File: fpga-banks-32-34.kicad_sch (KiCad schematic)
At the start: 11 parts, among them U4 XC7K160T-FFG676, Y3 Oscillator_100MHz_ASFL1

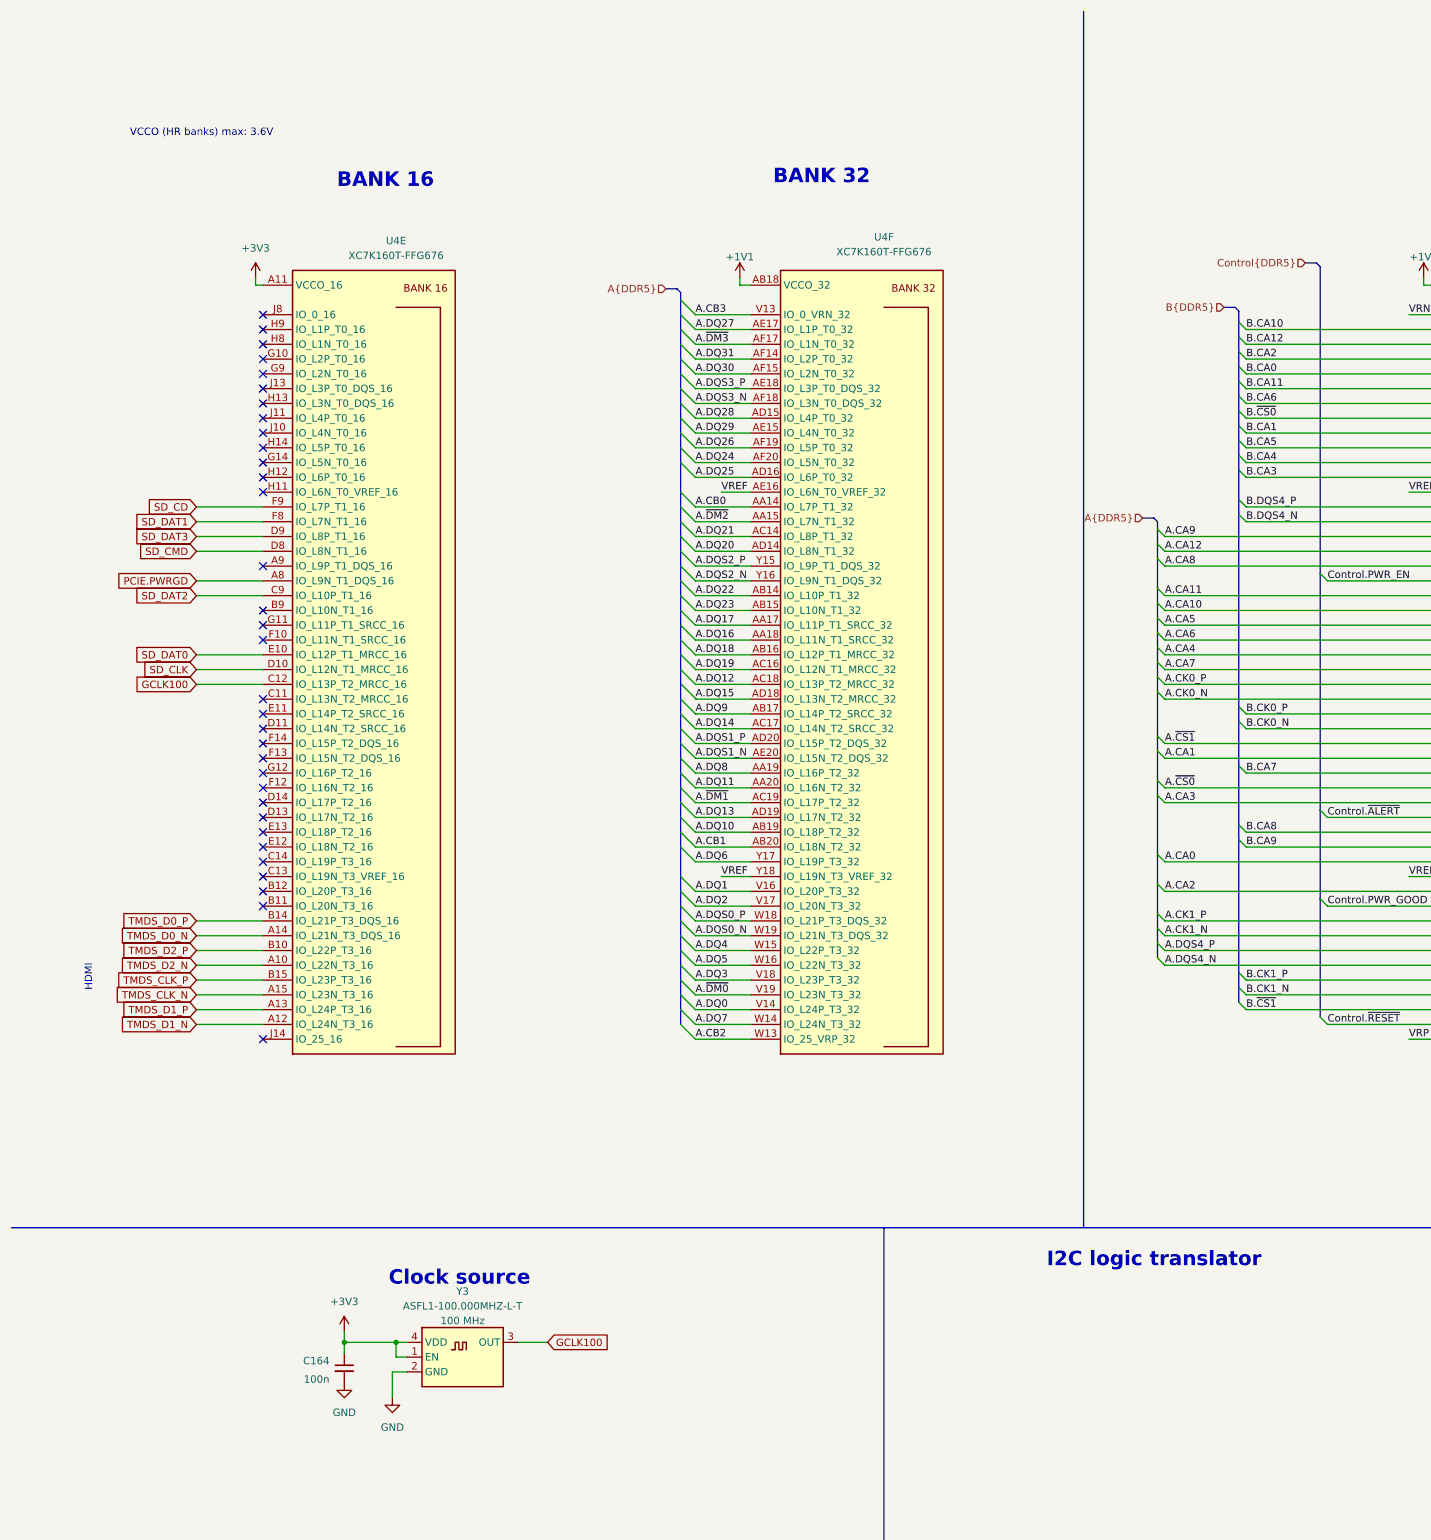
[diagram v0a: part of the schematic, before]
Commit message: Finish creating hierarchical buses and structure, start reconnecting signals
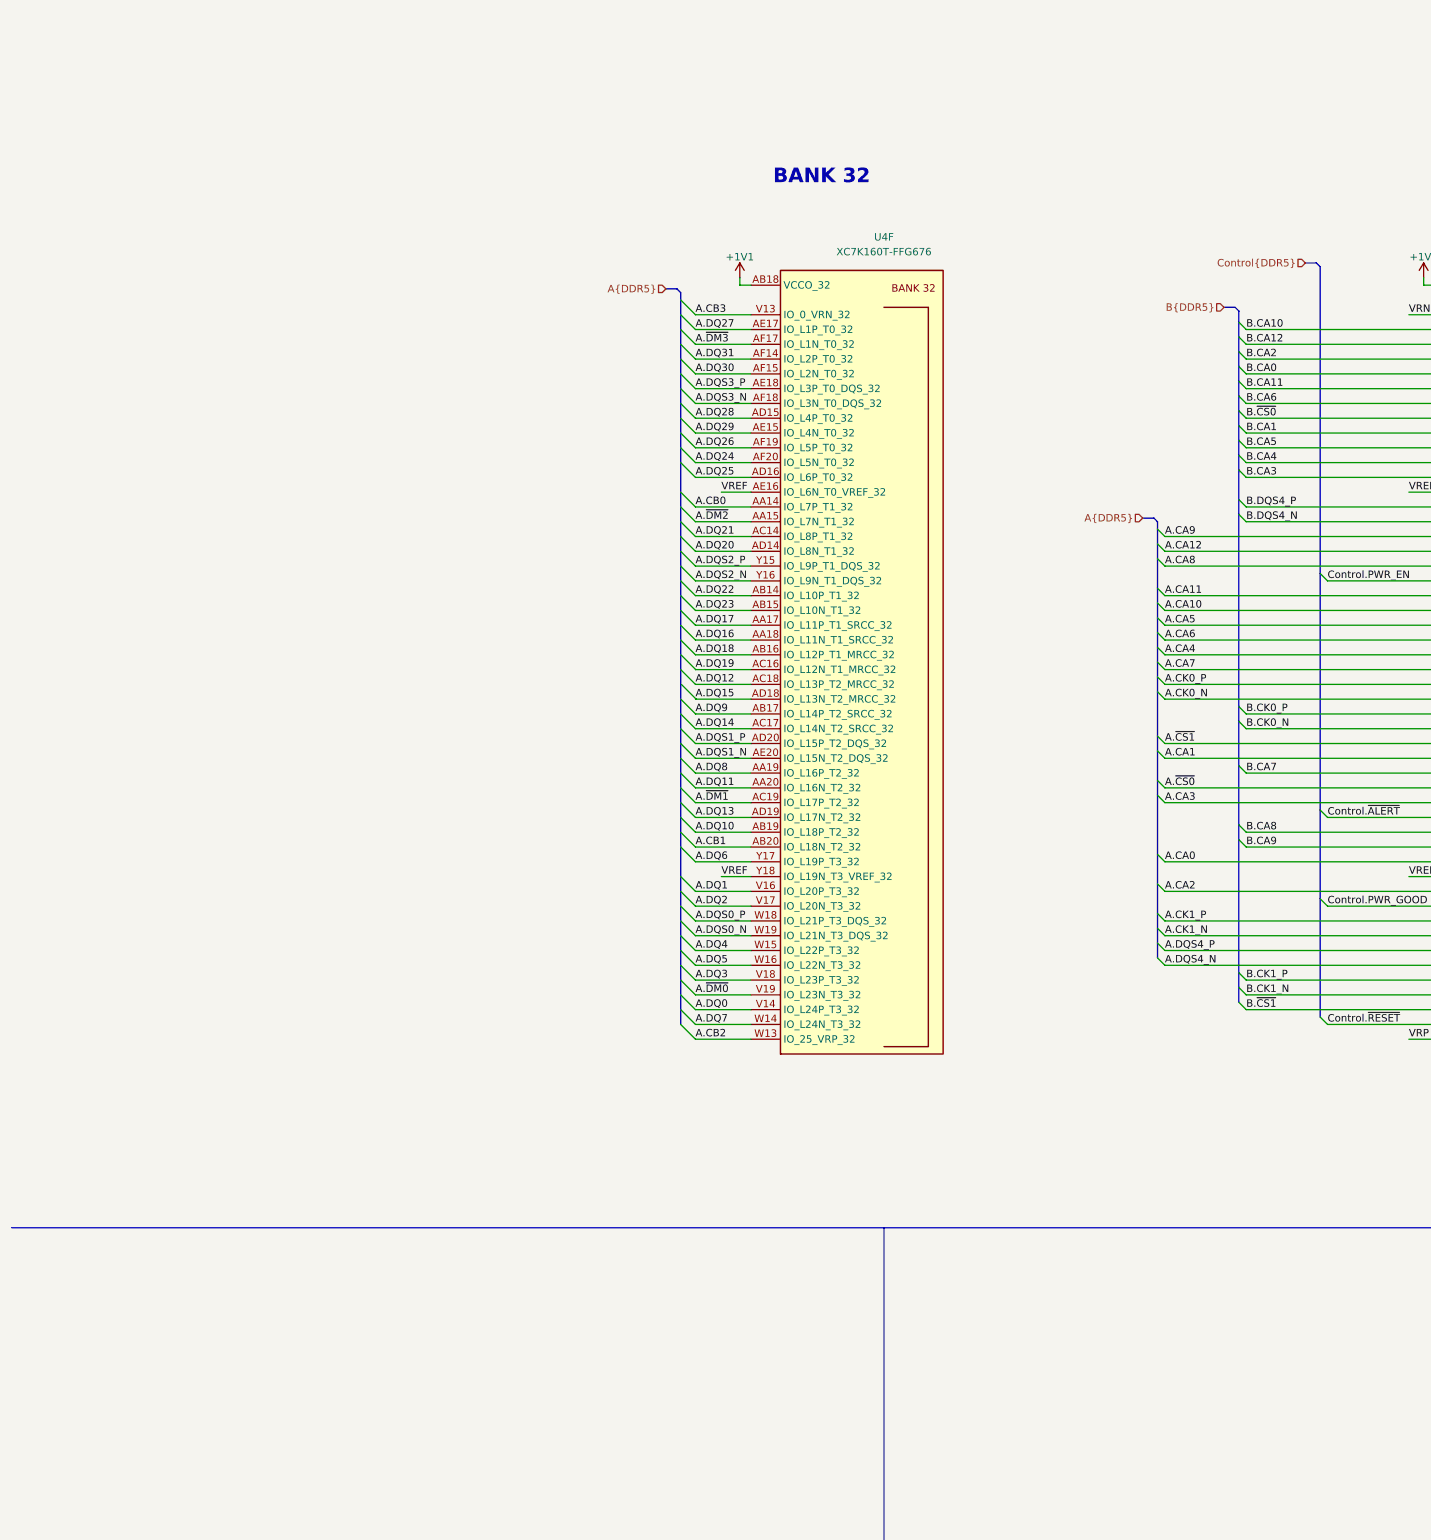
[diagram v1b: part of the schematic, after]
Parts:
- removed C164: C_100n_0402, sodimm-ddr5-tester-footprints:C_0402_1005Metric, symbol sodimm-ddr5-tester:C_100n_0402
- removed unit 5 of U4
- removed Y3: Oscillator_100MHz_ASFL1, sodimm-ddr5-tester-footprints:Oscillator_SMD_Abracon_ASFL1-4Pin_5.0x3.2mm, symbol sodimm-ddr5-tester:Oscillator_100MHz_ASFL1
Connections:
- no-connect marks 33 -> 0
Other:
- note removed: "BANK 16"
- note removed: "Clock source"
- note removed: "HDMI"
- note removed: "I2C logic translator"
- note removed: "VCCO (HR banks) max: 3.6V"

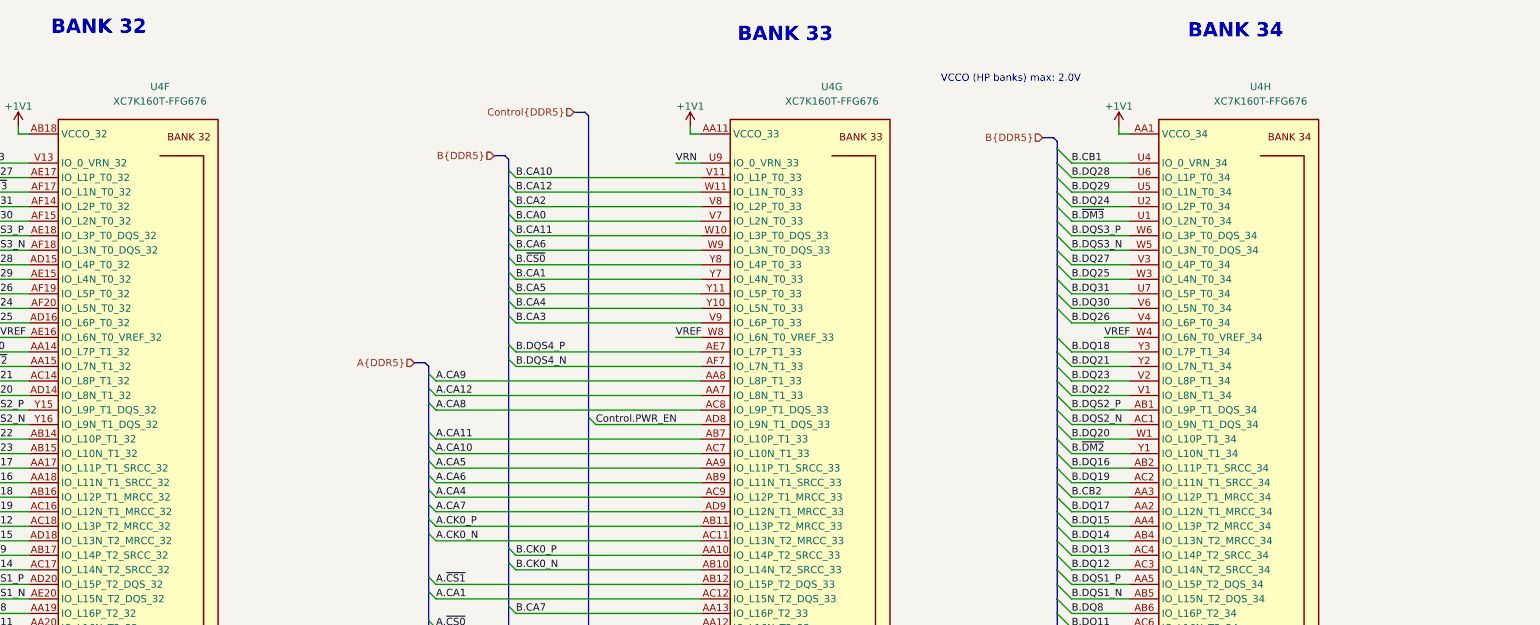
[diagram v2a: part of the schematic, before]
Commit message: Fix FPGA properties from the standardized library, update SO-DIMM symbol
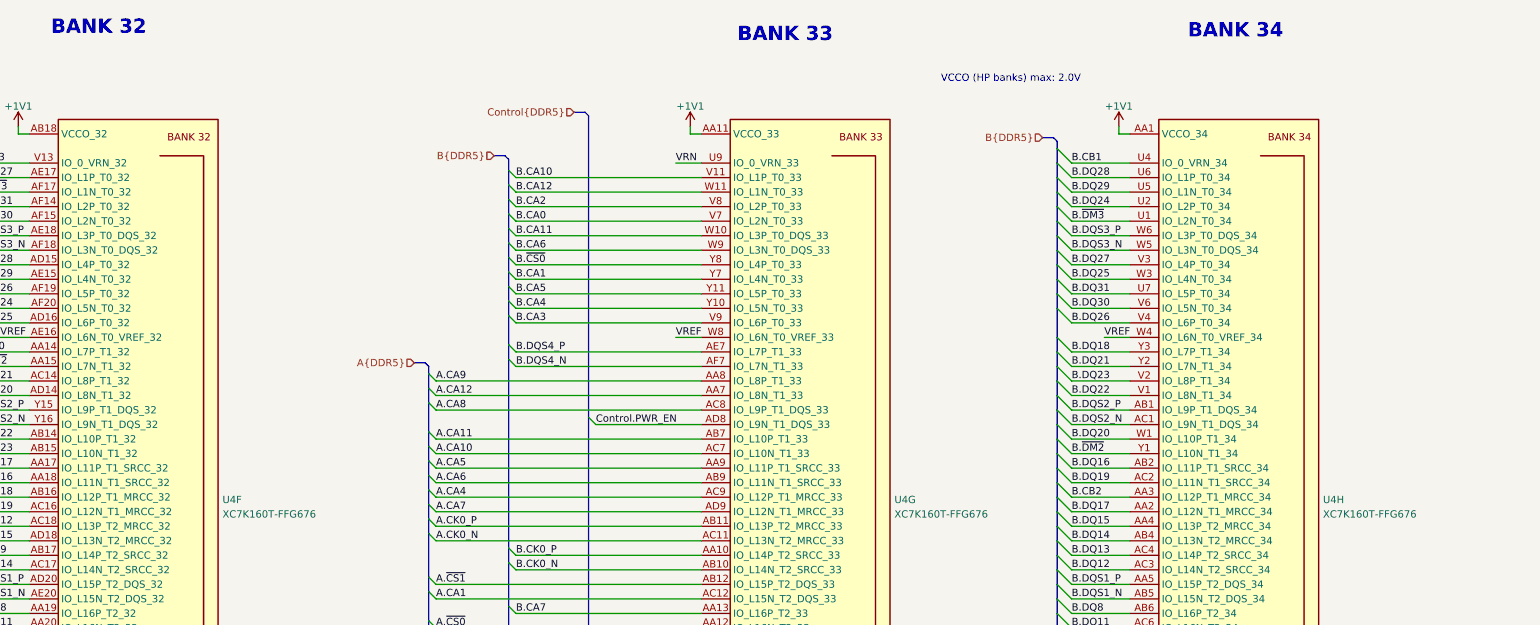
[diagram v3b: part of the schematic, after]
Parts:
- U4: footprint sodimm-ddr5-tester-footprints:BGA-676_27x27mm_Layout26x26_P1X1mm -> antmicro-footprints:BGA-676_27x27mm_Layout26x26_P1X1mm; symbol sodimm-ddr5-tester:XC7K160T-FFG676 -> antmicroMicrocontrollers:XC7K160T-FFG676; Manufacturer Xilinx -> AMD-Xilinx
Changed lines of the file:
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@@
     (effects (font (size 1.27 1.27)) (justify right))
   )
-  (symbol (lib_id "sodimm-ddr5-tester:XC7K160T-FFG676") (at 139.7 59.69 0) (unit 6)
+  (symbol (lib_id "antmicroMicrocontrollers:XC7K160T-FFG676") (at 139.7 59.69 0) (unit 6)
     (in_bom yes) (on_board yes) (fields_autoplaced)
-    (property "Reference" "U4" (id 0) (at 162.56 51.435 0))
-    (property "Value" "XC7K160T-FFG676" (id 1) (at 162.56 53.975 0)
-      (effects (font (size 1.27 1.27) (thickness 0.15)))
-    )
-    (property "Footprint" "sodimm-ddr5-tester-footprints:BGA-676_27x27mm_Layout26x26_P1X1mm" (id 2) (at 208.28 62.23 0)
+    (property "Reference" "U4" (id 0) (at 173.482 123.6294 0)
+      (effects (font (size 1.27 1.27)) (justify left))
+    )
+    (property "Value" "XC7K160T-FFG676" (id 1) (at 173.482 126.1597 0)
+      (effects (font (size 1.27 1.27) (thickness 0.15)) (justify left))
+    )
+    (property "Footprint" "antmicro-footprints:BGA-676_27x27mm_Layout26x26_P1X1mm" (id 2) (at 208.28 62.23 0)
       (effects (font (size 1.27 1.27) (thickness 0.15)) (justify left bottom) hide)
     )
@@
       (effects (font (size 1.27 1.27) (thickness 0.15)) (justify left bottom) hide)
     )
-    (property "Manufacturer" "Xilinx" (id 7) (at 139.7 59.69 0)
+    (property "Manufacturer" "AMD-Xilinx" (id 7) (at 139.7 59.69 0)
       (effects (font (size 1.27 1.27)) hide)
     )
@@
     (pin "1")
   )
-  (symbol (lib_id "sodimm-ddr5-tester:XC7K160T-FFG676") (at 257.175 59.69 0) (unit 7)
+  (symbol (lib_id "antmicroMicrocontrollers:XC7K160T-FFG676") (at 257.175 59.69 0) (unit 7)
     (in_bom yes) (on_board yes) (fields_autoplaced)
-    (property "Reference" "U4" (id 0) (at 280.035 51.435 0))
-    (property "Value" "XC7K160T-FFG676" (id 1) (at 280.035 53.975 0)
-      (effects (font (size 1.27 1.27) (thickness 0.15)))
-    )
-    (property "Footprint" "sodimm-ddr5-tester-footprints:BGA-676_27x27mm_Layout26x26_P1X1mm" (id 2) (at 325.755 62.23 0)
+    (property "Reference" "U4" (id 0) (at 290.957 123.6294 0)
+      (effects (font (size 1.27 1.27)) (justify left))
+    )
+    (property "Value" "XC7K160T-FFG676" (id 1) (at 290.957 126.1597 0)
+      (effects (font (size 1.27 1.27) (thickness 0.15)) (justify left))
+    )
+    (property "Footprint" "antmicro-footprints:BGA-676_27x27mm_Layout26x26_P1X1mm" (id 2) (at 325.755 62.23 0)
       (effects (font (size 1.27 1.27) (thickness 0.15)) (justify left bottom) hide)
     )
@@
       (effects (font (size 1.27 1.27) (thickness 0.15)) (justify left bottom) hide)
     )
-    (property "Manufacturer" "Xilinx" (id 7) (at 257.175 59.69 0)
+    (property "Manufacturer" "AMD-Xilinx" (id 7) (at 257.175 59.69 0)
       (effects (font (size 1.27 1.27)) hide)
     )
@@
     (pin "2")
   )
-  (symbol (lib_id "sodimm-ddr5-tester:XC7K160T-FFG676") (at 332.105 59.69 0) (unit 8)
+  (symbol (lib_id "antmicroMicrocontrollers:XC7K160T-FFG676") (at 332.105 59.69 0) (unit 8)
     (in_bom yes) (on_board yes) (fields_autoplaced)
-    (property "Reference" "U4" (id 0) (at 354.965 51.435 0))
-    (property "Value" "XC7K160T-FFG676" (id 1) (at 354.965 53.975 0)
-      (effects (font (size 1.27 1.27) (thickness 0.15)))
-    )
-    (property "Footprint" "sodimm-ddr5-tester-footprints:BGA-676_27x27mm_Layout26x26_P1X1mm" (id 2) (at 400.685 62.23 0)
+    (property "Reference" "U4" (id 0) (at 365.887 123.6294 0)
+      (effects (font (size 1.27 1.27)) (justify left))
+    )
+    (property "Value" "XC7K160T-FFG676" (id 1) (at 365.887 126.1597 0)
+      (effects (font (size 1.27 1.27) (thickness 0.15)) (justify left))
+    )
+    (property "Footprint" "antmicro-footprints:BGA-676_27x27mm_Layout26x26_P1X1mm" (id 2) (at 400.685 62.23 0)
       (effects (font (size 1.27 1.27) (thickness 0.15)) (justify left bottom) hide)
     )
@@
       (effects (font (size 1.27 1.27) (thickness 0.15)) (justify left bottom) hide)
     )
-    (property "Manufacturer" "Xilinx" (id 7) (at 332.105 59.69 0)
-      (effects (font (size 1.27 1.27)) hide)
-    )
+    (property "Manufacturer" "AMD-Xilinx" (id 7) (at 332.105 59.69 0)
+      (effects (font (size 1.27 1.27)) hide)
+    )

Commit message: Loclib of the project
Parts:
- U4: footprint antmicro-footprints:BGA-676_27x27mm_Layout26x26_P1X1mm -> sodimm-ddr5-tester-footprints:BGA-676_27x27mm_Layout26x26_P1X1mm; symbol antmicroMicrocontrollers:XC7K160T-FFG676 -> sodimm-ddr5-tester:XC7K160T-FFG676

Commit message: Finish schematic cleanup
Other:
- note added: "HP Banks"
- note added: "Pinout D.1.1"
- note added: "Reference termination"
- moved on the sheet: C167, C168, R129, R130, R131, R132, R133, R134, U4F, U4G, U4H
